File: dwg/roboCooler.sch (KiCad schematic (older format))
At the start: 46 parts, among them J1 CONN_01X02, J10 CONN_02X03, J11 CONN_01X04, J12 USB_A, J13 CONN_02X03, J14 CONN_02X03, J2 CONN_01X02, J3 Discovery_F407_P1, J4 CONN_01X06, J5 CONN_01X12, J6 Discovery_F407_P2, J7 CONN_02X03, J8 CONN_02X03, Q1 NMOS, Q2 NMOS, U1 SN74LV, U2 TB6549

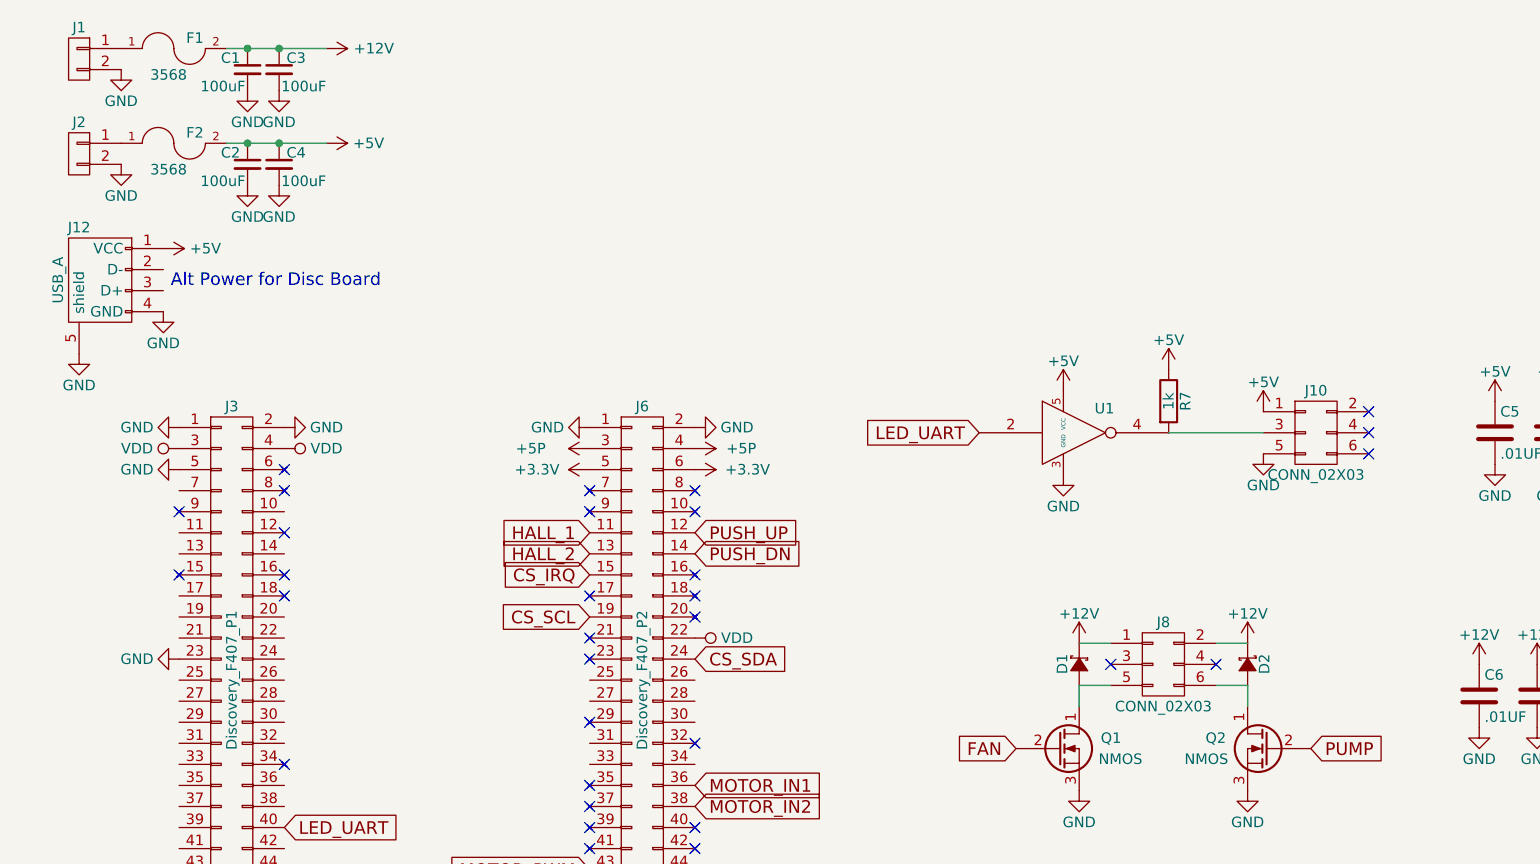
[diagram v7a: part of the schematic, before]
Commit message: added 8 leds
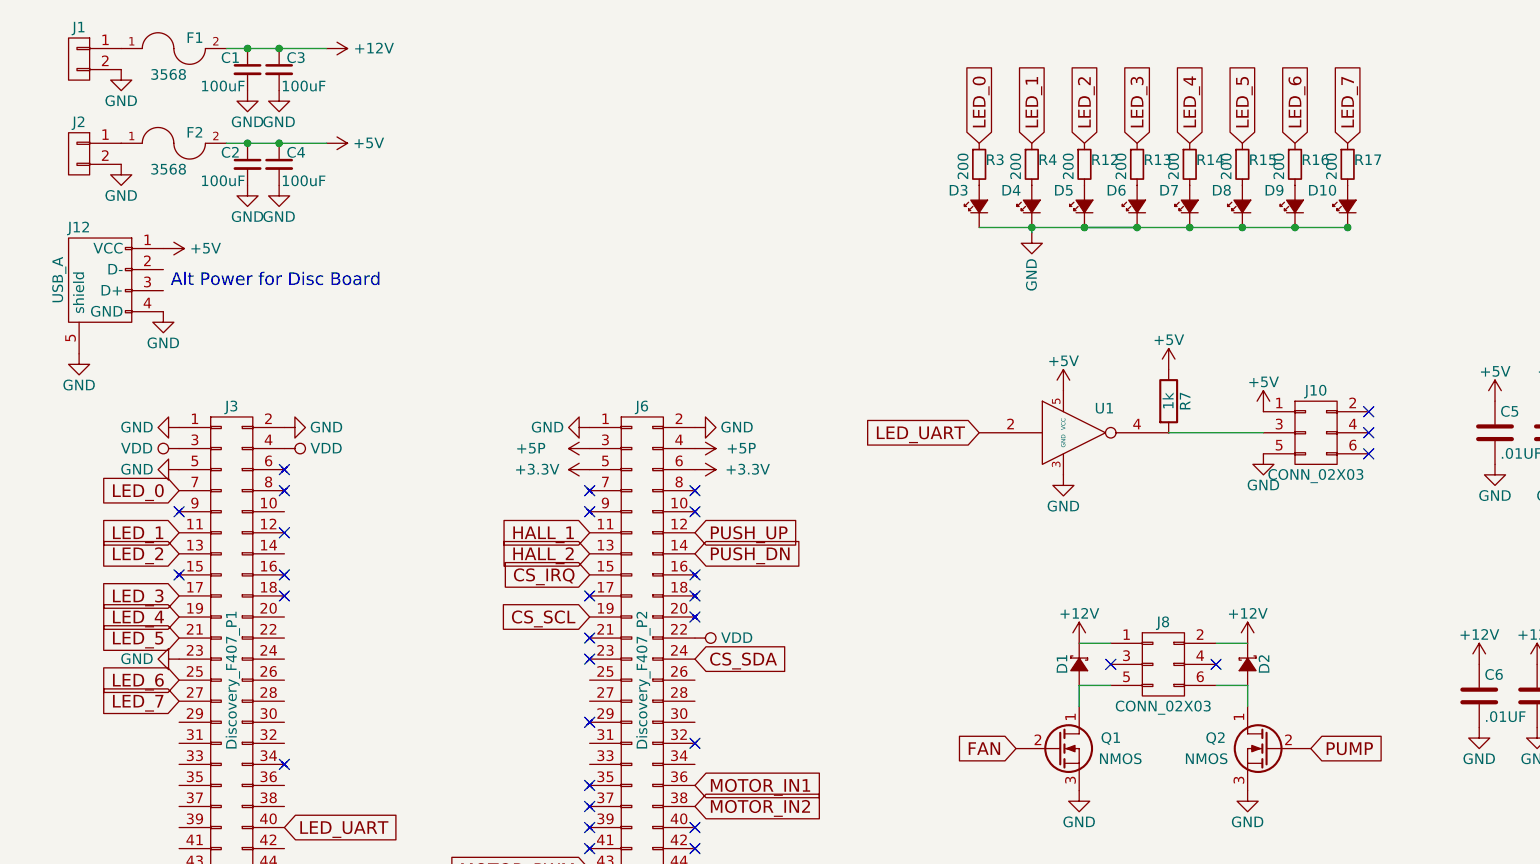
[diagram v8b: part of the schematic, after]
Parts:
- added D10, D3, D4, D5, D6, D7, D8, D9: Led_Small, Resistors_SMD:R_0805_HandSoldering, symbol Led_Small
- added R12, R13, R14, R15, R16, R17, R3, R4: 200, Resistors_SMD:R_0805_HandSoldering, symbol R_Small
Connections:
- net GND: now also D10.1 (K), D3.1 (K), D4.1 (K), D5.1 (K), D6.1 (K), D7.1 (K), D8.1 (K), D9.1 (K)
- net LED_1: now reaches J3.11 (P11)
- net LED_1: now also R4.1
- net LED_2: now reaches J3.13 (P13)
- net LED_2: now also R12.1
- net LED_3: now reaches J3.17 (P17)
- net LED_3: now also R13.1
- net LED_4: now reaches J3.19 (P19)
- net LED_4: now also R14.1
- net LED_5: now reaches J3.21 (P21)
- net LED_5: now also R15.1
- net LED_6: now reaches J3.25 (P25)
- net LED_6: now also R16.1
- net LED_7: now reaches J3.27 (P27)
- net LED_7: now also R17.1
- net LED_0: now reaches J3.7 (P7)
- net LED_0: now also R3.1
- new net: D3.2 (A), R3.2
- new net: D4.2 (A), R4.2
- new net: D5.2 (A), R12.2
- new net: D6.2 (A), R13.2
- new net: D7.2 (A), R14.2
- new net: D8.2 (A), R15.2
- new net: D9.2 (A), R16.2
- new net: D10.2 (A), R17.2
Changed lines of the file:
@@
 NoConn ~ 6875 2475
 NoConn ~ 6875 2375
+$Comp
+L R_Small R3
+U 1 1 57846A87
+P 5025 1200
+F 0 "R3" H 5055 1220 50  0000 L CNN
+F 1 "200" V 4950 1125 50  0000 L CNN
+F 2 "Resistors_SMD:R_0805_HandSoldering" H 5025 1200 50  0001 C CNN
+F 3 "" H 5025 1200 50  0000 C CNN
+	1    5025 1200
+	1    0    0    -1
+$EndComp
+$Comp
+L Led_Small D3
+U 1 1 57846B2C
+P 5025 1400
+F 0 "D3" V 5100 1450 50  0000 L CNN
+F 1 "Led_Small" H 4850 1300 50  0001 L CNN
+F 2 "Resistors_SMD:R_0805_HandSoldering" V 5025 1400 50  0001 C CNN
+F 3 "" V 5025 1400 50  0000 C CNN
+	1    5025 1400
+	0    -1   -1   0
+$EndComp
+$Comp
+L R_Small R4
+U 1 1 578498BB
+P 5275 1200
+F 0 "R4" H 5305 1220 50  0000 L CNN
+F 1 "200" V 5200 1125 50  0000 L CNN
+F 2 "Resistors_SMD:R_0805_HandSoldering" H 5275 1200 50  0001 C CNN
+F 3 "" H 5275 1200 50  0000 C CNN
+	1    5275 1200
+	1    0    0    -1
+$EndComp
+$Comp
+L Led_Small D4
+U 1 1 578498C1
+P 5275 1400
+F 0 "D4" V 5350 1450 50  0000 L CNN
+F 1 "Led_Small" H 5100 1300 50  0001 L CNN
+F 2 "Resistors_SMD:R_0805_HandSoldering" V 5275 1400 50  0001 C CNN
+F 3 "" V 5275 1400 50  0000 C CNN
+	1    5275 1400
+	0    -1   -1   0
+$EndComp
+$Comp
+L GND #PWR068
+U 1 1 578498C7
+P 5275 1525
+F 0 "#PWR068" H 5275 1275 50  0001 C CNN
+F 1 "GND" V 5275 1325 50  0000 C CNN
+F 2 "" H 5275 1525 60  0000 C CNN
+F 3 "" H 5275 1525 60  0000 C CNN
+	1    5275 1525
+	-1   0    0    -1
+$EndComp
+Wire Wire Line
+	5025 1500 6775 1500
+Wire Wire Line
+	5275 1500 5275 1525
+$Comp
+L R_Small R12
+U 1 1 5784AFD6
+P 5525 1200
+F 0 "R12" H 5555 1220 50  0000 L CNN
+F 1 "200" V 5450 1125 50  0000 L CNN
+F 2 "Resistors_SMD:R_0805_HandSoldering" H 5525 1200 50  0001 C CNN
+F 3 "" H 5525 1200 50  0000 C CNN
+	1    5525 1200
+	1    0    0    -1
+$EndComp
+$Comp
+L Led_Small D5
+U 1 1 5784AFDC
+P 5525 1400
+F 0 "D5" V 5600 1450 50  0000 L CNN
+F 1 "Led_Small" H 5350 1300 50  0001 L CNN
+F 2 "Resistors_SMD:R_0805_HandSoldering" V 5525 1400 50  0001 C CNN
+F 3 "" V 5525 1400 50  0000 C CNN
+	1    5525 1400
+	0    -1   -1   0
+$EndComp
+Connection ~ 5525 1500
+Connection ~ 5275 1500
+$Comp
+L R_Small R13
+U 1 1 5784B579
+P 5775 1200
+F 0 "R13" H 5805 1220 50  0000 L CNN
+F 1 "200" V 5700 1125 50  0000 L CNN
+F 2 "Resistors_SMD:R_0805_HandSoldering" H 5775 1200 50  0001 C CNN
+F 3 "" H 5775 1200 50  0000 C CNN
+	1    5775 1200
+	1    0    0    -1
+$EndComp
+$Comp
+L Led_Small D6
+U 1 1 5784B57F
+P 5775 1400
+F 0 "D6" V 5850 1450 50  0000 L CNN
+F 1 "Led_Small" H 5600 1300 50  0001 L CNN
+F 2 "Resistors_SMD:R_0805_HandSoldering" V 5775 1400 50  0001 C CNN
+F 3 "" V 5775 1400 50  0000 C CNN
+	1    5775 1400
+	0    -1   -1   0
+$EndComp
+$Comp
+L R_Small R14
+U 1 1 5784B585
+P 6025 1200
+F 0 "R14" H 6055 1220 50  0000 L CNN
+F 1 "200" V 5950 1125 50  0000 L CNN
+F 2 "Resistors_SMD:R_0805_HandSoldering" H 6025 1200 50  0001 C CNN
+F 3 "" H 6025 1200 50  0000 C CNN
+	1    6025 1200
+	1    0    0    -1
+$EndComp
+$Comp
+L Led_Small D7
+U 1 1 5784B58B
+P 6025 1400
+F 0 "D7" V 6100 1450 50  0000 L CNN
+F 1 "Led_Small" H 5850 1300 50  0001 L CNN
+F 2 "Resistors_SMD:R_0805_HandSoldering" V 6025 1400 50  0001 C CNN
+F 3 "" V 6025 1400 50  0000 C CNN
+	1    6025 1400
+	0    -1   -1   0
+$EndComp
+$Comp
+L R_Small R15
+U 1 1 5784B599
+P 6275 1200
+F 0 "R15" H 6305 1220 50  0000 L CNN
+F 1 "200" V 6200 1125 50  0000 L CNN
+F 2 "Resistors_SMD:R_0805_HandSoldering" H 6275 1200 50  0001 C CNN
+F 3 "" H 6275 1200 50  0000 C CNN
+	1    6275 1200
+	1    0    0    -1
+$EndComp
+$Comp
+L Led_Small D8
+U 1 1 5784B59F
+P 6275 1400
+F 0 "D8" V 6350 1450 50  0000 L CNN
+F 1 "Led_Small" H 6100 1300 50  0001 L CNN
+F 2 "Resistors_SMD:R_0805_HandSoldering" V 6275 1400 50  0001 C CNN
+F 3 "" V 6275 1400 50  0000 C CNN
+	1    6275 1400
+	0    -1   -1   0
+$EndComp
+Connection ~ 6275 1500
+Connection ~ 6025 1500
+$Comp
+L R_Small R16
+U 1 1 5784B8D6
+P 6525 1200
+F 0 "R16" H 6555 1220 50  0000 L CNN
+F 1 "200" V 6450 1125 50  0000 L CNN
+F 2 "Resistors_SMD:R_0805_HandSoldering" H 6525 1200 50  0001 C CNN
+F 3 "" H 6525 1200 50  0000 C CNN
+	1    6525 1200
+	1    0    0    -1
+$EndComp
+$Comp
+L Led_Small D9
+U 1 1 5784B8DC
+P 6525 1400
+F 0 "D9" V 6600 1450 50  0000 L CNN
+F 1 "Led_Small" H 6350 1300 50  0001 L CNN
+F 2 "Resistors_SMD:R_0805_HandSoldering" V 6525 1400 50  0001 C CNN
+F 3 "" V 6525 1400 50  0000 C CNN
+	1    6525 1400
+	0    -1   -1   0
+$EndComp
+$Comp
+L R_Small R17
+U 1 1 5784B8E2
+P 6775 1200
+F 0 "R17" H 6805 1220 50  0000 L CNN
+F 1 "200" V 6700 1125 50  0000 L CNN
+F 2 "Resistors_SMD:R_0805_HandSoldering" H 6775 1200 50  0001 C CNN
+F 3 "" H 6775 1200 50  0000 C CNN
+	1    6775 1200
+	1    0    0    -1
+$EndComp
+$Comp
+L Led_Small D10
+U 1 1 5784B8E8
+P 6775 1400
+F 0 "D10" V 6850 1450 50  0000 L CNN
+F 1 "Led_Small" H 6600 1300 50  0001 L CNN
+F 2 "Resistors_SMD:R_0805_HandSoldering" V 6775 1400 50  0001 C CNN
+F 3 "" V 6775 1400 50  0000 C CNN
+	1    6775 1400
+	0    -1   -1   0
+$EndComp
+Connection ~ 6525 1500
+Wire Wire Line
+	5525 1500 5775 1500
+Connection ~ 5775 1500
+Connection ~ 6775 1500
+Text GLabel 5275 1100 1    60   Input ~ 0
+LED_1
+Text GLabel 5525 1100 1    60   Input ~ 0
+LED_2
+Text GLabel 5775 1100 1    60   Input ~ 0
+LED_3
+Text GLabel 6025 1100 1    60   Input ~ 0
+LED_4
+Text GLabel 6275 1100 1    60   Input ~ 0
+LED_5
+Text GLabel 6525 1100 1    60   Input ~ 0
+LED_6
+Text GLabel 6775 1100 1    60   Input ~ 0
+LED_7
+Text GLabel 5025 1100 1    60   Input ~ 0
+LED_0
+Text GLabel 1225 2950 0    60   Input ~ 0
+LED_1
+Text GLabel 1225 3050 0    60   Input ~ 0
+LED_2
+Text GLabel 1225 3250 0    60   Input ~ 0
+LED_3
+Text GLabel 1225 3350 0    60   Input ~ 0
+LED_4
+Text GLabel 1225 3450 0    60   Input ~ 0
+LED_5
+Text GLabel 1225 3650 0    60   Input ~ 0
+LED_6
+Text GLabel 1225 3750 0    60   Input ~ 0
+LED_7
+Text GLabel 1225 2750 0    60   Input ~ 0
+LED_0
 $EndSCHEMATC
